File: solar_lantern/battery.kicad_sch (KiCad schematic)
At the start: 7 parts

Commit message: Nicen schematics a bit
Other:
- company: (none) -> Catnip electronics
- title: (none) -> Battery interconnect
- moved on the sheet: BT1, BT2, BT3, JP1, JP2, R20, R21

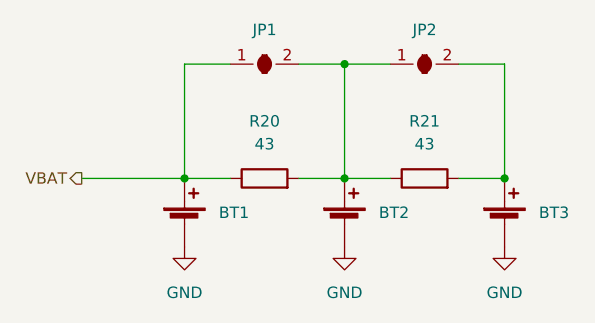
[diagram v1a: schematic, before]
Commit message: Add CERN-OHL_S licence
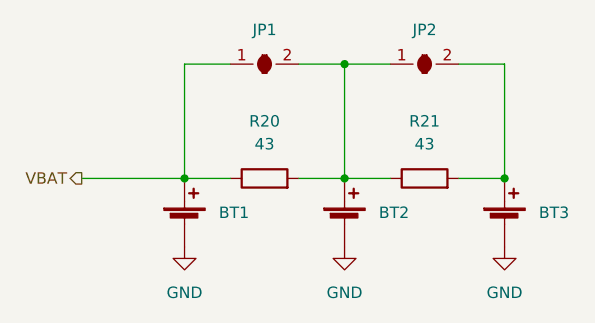
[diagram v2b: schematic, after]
